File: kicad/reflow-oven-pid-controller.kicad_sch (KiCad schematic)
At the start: 31 parts, among them J1 1x2P - 5.08mm, J2 1x2P - 5.08mm, J4 1x4P - 2.54mm, J5 1x4P - Right-Angle, J6 1x2P - 5.08mm, Q1 60V - 300mA, Q2 60V - 300mA, U1 3.3v - 500mA, U2 32KB - ARM-M0, U3 1 Channel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

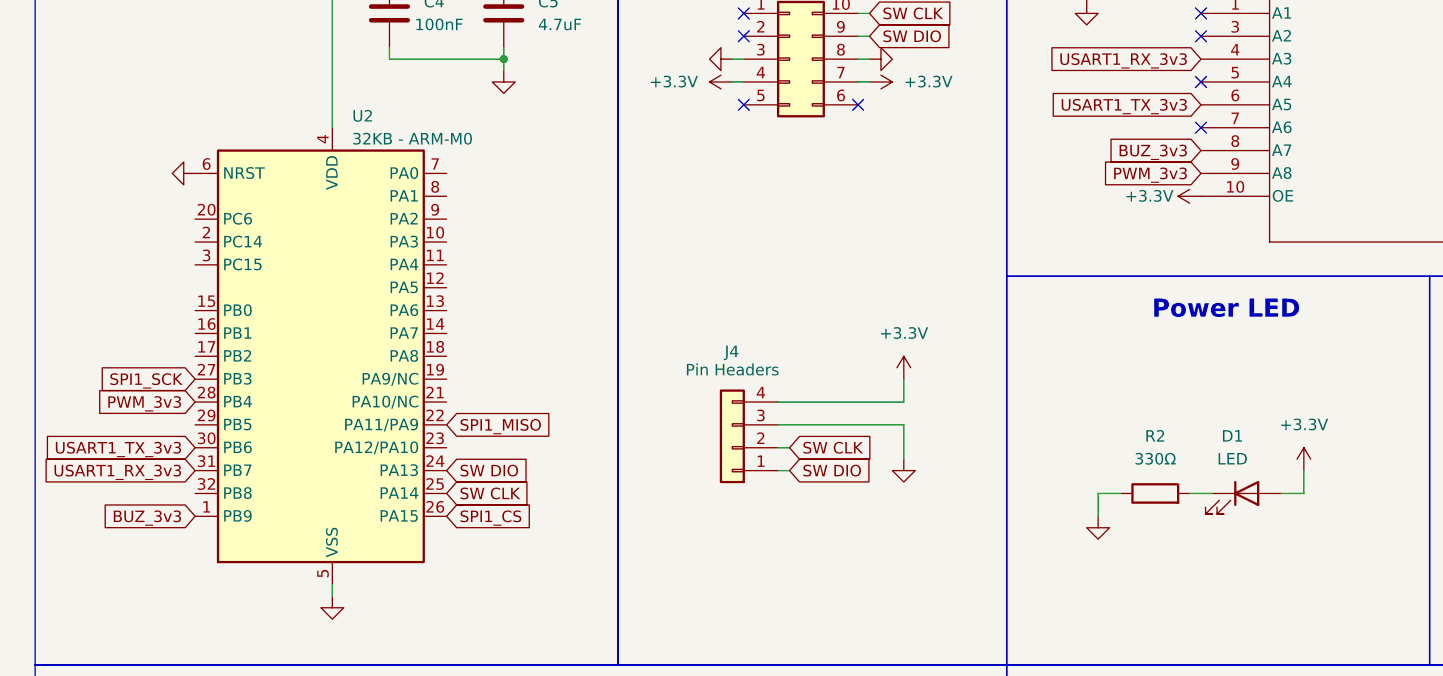
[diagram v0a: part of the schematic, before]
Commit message: Hardware updates
* Made adjustments for easier hand solder, More spacing and added thermal reliefs
* Changed LDO component  as selected wrong footprint for old one.
* Moved power led to top of board
* Changed power led resistor to hopefully make led less bright
* Added cap to MCU NRST as this was somehow forgotten rendering the MCU none working.
* Adjusted screw terminal footprints slightly as board overhand was too much.
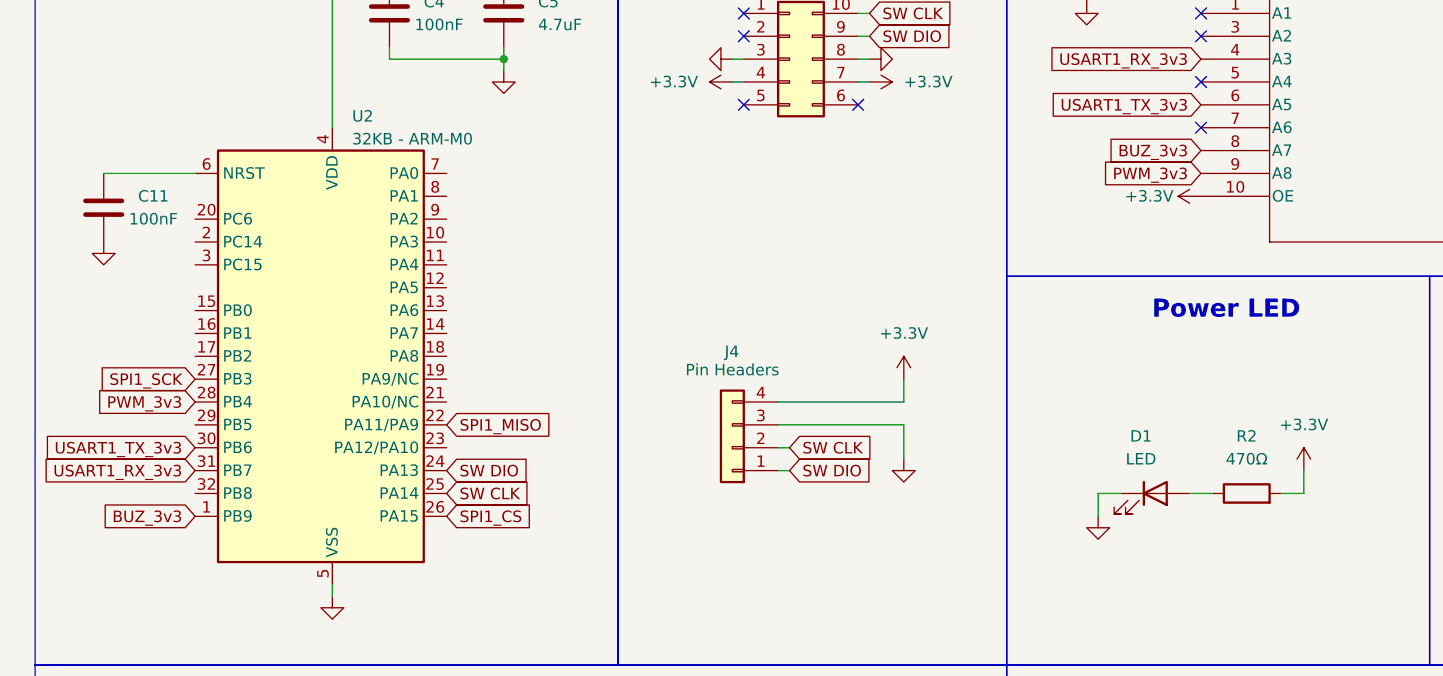
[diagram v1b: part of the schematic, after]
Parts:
- added C11: 100nF, Capacitor_SMD:C_0805_2012Metric, symbol Device:C
- R2: value 330Ω -> 470Ω; LCSC C17630 -> C17710; Part Number 0805W8F3300T5E -> 0805W8F4700T5E
- U1: LCSC C5884134 -> C347222; Manufacturer DSTECH -> UMW(Youtai Semiconductor Co., Ltd.); Part Number DS8242-33SS3 -> AMS1117-3.3
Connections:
- net +3.3V: now also R2.2; no longer D1.2 (A)
- net GND: now also D1.1 (K), C11.2; no longer R2.1, U2.6 (NRST)
- new net: C11.1, U2.6 (NRST)
- new net: D1.2 (A), R2.1
